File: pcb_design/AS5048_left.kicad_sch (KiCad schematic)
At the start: 6 parts, among them J5 AS5600_Right, U7 AS5048B-HTSP

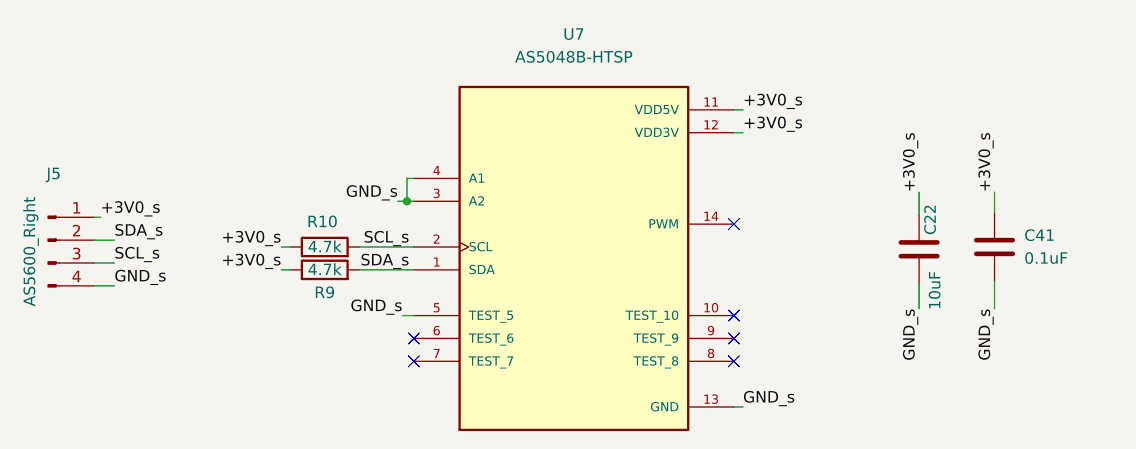
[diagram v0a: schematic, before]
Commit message: modified capacitors for encoders
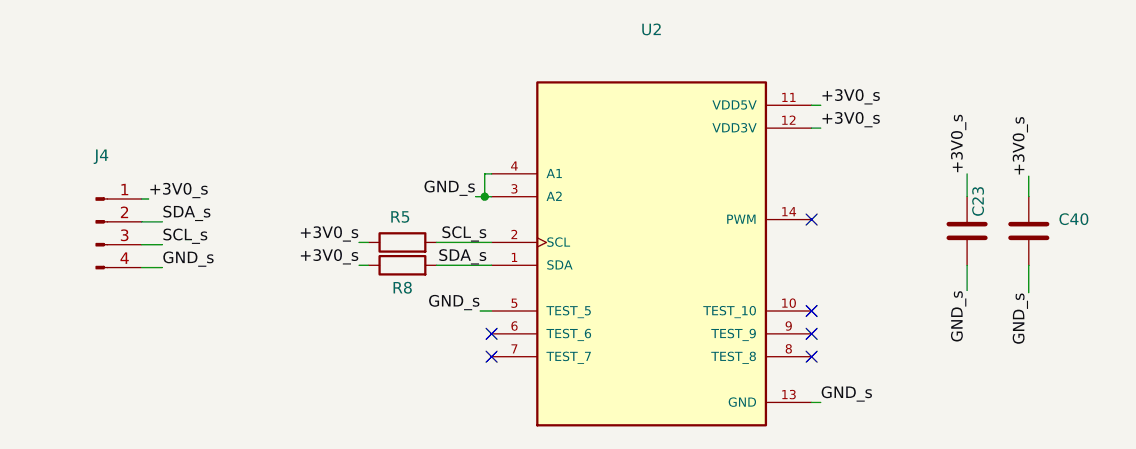
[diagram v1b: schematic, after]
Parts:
- removed C22: 10uF, Capacitor_SMD:C_0603_1608Metric, symbol Device:C
- removed C41: 0.1uF, Capacitor_SMD:C_0402_1005Metric, symbol Device:C
- removed J5: AS5600_Right, mushak_mount_footprint:STAND_SLAVE_04, symbol Connector:Conn_01x04_Male
- removed R10, R9: 4.7k, Resistor_SMD:R_0402_1005Metric, symbol Device:R
- removed U7: AS5048B-HTSP, AS5048B-HTSP:SOP65P640X120-14N, symbol AS5048B-HTSP:AS5048B-HTSP
- added C23, C40: (no value), symbol Device:C
- added J4: (no value), symbol Connector:Conn_01x04_Male
- added R5, R8: (no value), symbol Device:R
- added U2: (no value), symbol AS5048B-HTSP:AS5048B-HTSP
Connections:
- net +3V0_s: now also C23.2, C40.1, J4.1 (Pin_1), R5.1, R8.1, U2.11 (VDD5V), U2.12 (VDD3V)
- net GND_s: now also C23.1, C40.2, J4.4 (Pin_4), U2.13 (GND), U2.3 (A2), U2.4 (A1), U2.5 (TEST_5)
- net SCL_s: now also J4.3 (Pin_3), R5.2, U2.2 (SCL)
- net SDA_s: now also J4.2 (Pin_2), R8.2, U2.1 (SDA)

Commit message: Add resistors between MOSFET gate
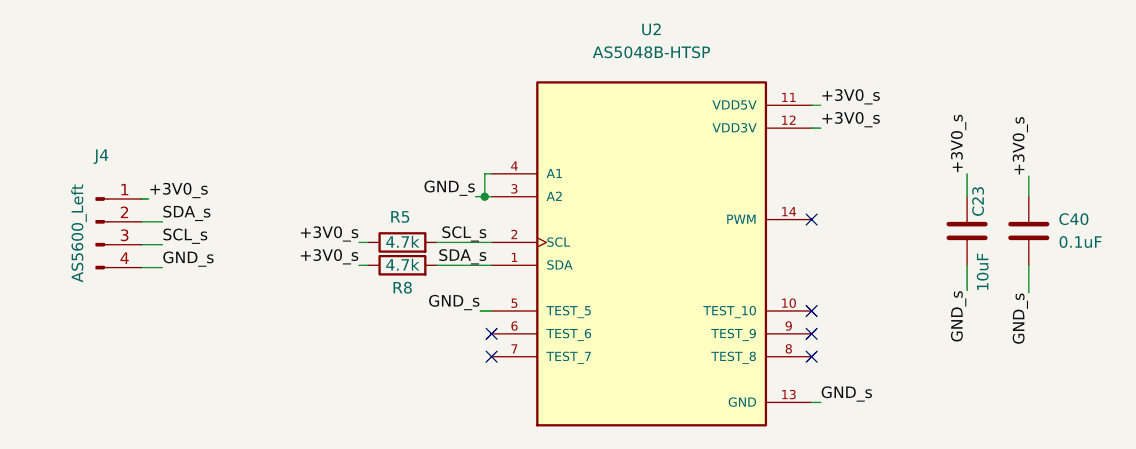
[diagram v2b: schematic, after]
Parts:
- C23: value (none) -> 10uF; footprint (none) -> Capacitor_SMD:C_0603_1608Metric
- C40: value (none) -> 0.1uF; footprint (none) -> Capacitor_SMD:C_0402_1005Metric
- J4: value (none) -> AS5600_Left; footprint (none) -> mushak_mount_footprint:STAND_SLAVE_04
- R5, R8: value (none) -> 4.7k; footprint (none) -> Resistor_SMD:R_0402_1005Metric
- U2: value (none) -> AS5048B-HTSP; footprint (none) -> AS5048B-HTSP:SOP65P640X120-14N
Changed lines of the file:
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@@
     (in_bom yes) (on_board yes)
     (property "Reference" "C23" (id 0) (at 208.28 92.964 90))
-    (property "Value" "" (id 1) (at 208.788 100.838 90))
-    (property "Footprint" "" (id 2) (at 206.0448 92.456 0)
+    (property "Value" "10uF" (id 1) (at 208.788 100.838 90))
+    (property "Footprint" "Capacitor_SMD:C_0603_1608Metric" (id 2) (at 206.0448 92.456 0)
       (effects (font (size 1.27 1.27)) hide)
     )
@@
       (effects (font (size 1.27 1.27)) (justify left))
     )
-    (property "Value" "" (id 1) (at 217.17 97.5359 0)
+    (property "Value" "0.1uF" (id 1) (at 217.17 97.5359 0)
       (effects (font (size 1.27 1.27)) (justify left))
     )
-    (property "Footprint" "" (id 2) (at 214.8332 100.076 0)
+    (property "Footprint" "Capacitor_SMD:C_0402_1005Metric" (id 2) (at 214.8332 100.076 0)
       (effects (font (size 1.27 1.27)) hide)
     )
@@
     (in_bom yes) (on_board yes) (fields_autoplaced)
     (property "Reference" "U2" (id 0) (at 171.958 73.914 0))
-    (property "Value" "" (id 1) (at 171.958 76.454 0))
-    (property "Footprint" "" (id 2) (at 171.958 97.536 0)
+    (property "Value" "AS5048B-HTSP" (id 1) (at 171.958 76.454 0))
+    (property "Footprint" "AS5048B-HTSP:SOP65P640X120-14N" (id 2) (at 171.958 97.536 0)
       (effects (font (size 1.27 1.27)) (justify left bottom) hide)
     )
@@
     (in_bom yes) (on_board yes)
     (property "Reference" "R8" (id 0) (at 144.272 102.616 90))
-    (property "Value" "" (id 1) (at 144.272 100.076 90))
-    (property "Footprint" "" (id 2) (at 144.272 101.854 90)
+    (property "Value" "4.7k" (id 1) (at 144.272 100.076 90))
+    (property "Footprint" "Resistor_SMD:R_0402_1005Metric" (id 2) (at 144.272 101.854 90)
       (effects (font (size 1.27 1.27)) hide)
     )
@@
     (in_bom yes) (on_board yes)
     (property "Reference" "J4" (id 0) (at 110.871 87.884 0))
-    (property "Value" "" (id 1) (at 108.204 96.52 90))
-    (property "Footprint" "" (id 2) (at 110.236 95.25 0)
+    (property "Value" "AS5600_Left" (id 1) (at 108.204 96.52 90))
+    (property "Footprint" "mushak_mount_footprint:STAND_SLAVE_04" (id 2) (at 110.236 95.25 0)
       (effects (font (size 1.27 1.27)) hide)
     )
@@
     (in_bom yes) (on_board yes)
     (property "Reference" "R5" (id 0) (at 144.018 94.742 90))
-    (property "Value" "" (id 1) (at 144.272 97.536 90))
-    (property "Footprint" "" (id 2) (at 144.272 99.314 90)
+    (property "Value" "4.7k" (id 1) (at 144.272 97.536 90))
+    (property "Footprint" "Resistor_SMD:R_0402_1005Metric" (id 2) (at 144.272 99.314 90)
       (effects (font (size 1.27 1.27)) hide)
     )

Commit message: Update Mushak PCB design to include new features (#5)
* Update mushak PCB with new changes
* Add AMS1117 as 3.3v regulator
* Add new alternate placement for IR sensors
* Add new 3.3v compatible ToF sensor
* Update gerber files

* Add changes to silkscreen and filter capacitors
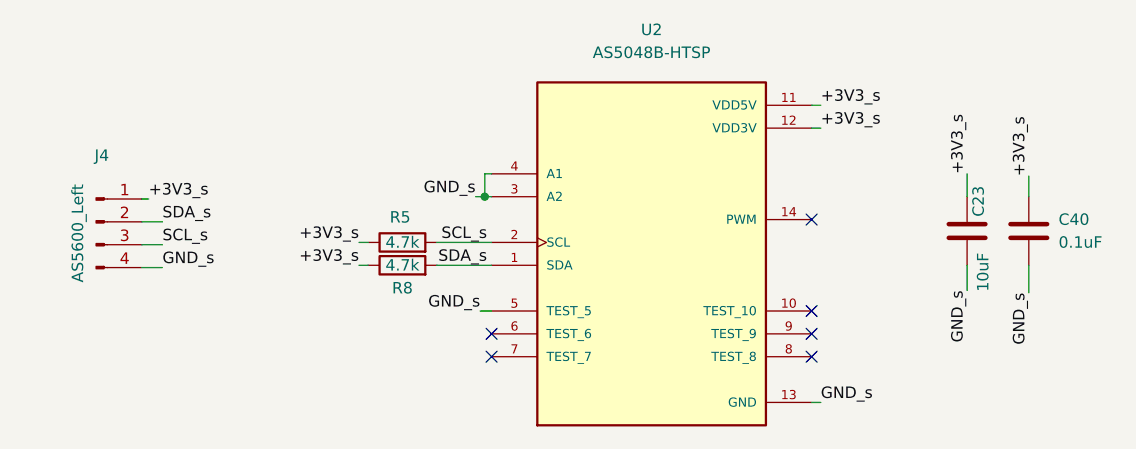
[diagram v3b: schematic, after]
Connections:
- net +3V0_s renamed +3V3_s
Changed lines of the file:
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@@
     (effects (font (size 1.27 1.27)) (justify right bottom))
   )
-  (label "+3V0_s" (at 190.754 82.296 0)
+  (label "+3V3_s" (at 190.754 82.296 0)
     (effects (font (size 1.27 1.27)) (justify left bottom))
   )
@@
     (effects (font (size 1.27 1.27)) (justify right bottom))
   )
-  (label "+3V0_s" (at 207.01 89.916 90)
+  (label "+3V3_s" (at 207.01 89.916 90)
     (effects (font (size 1.27 1.27)) (justify left bottom))
   )
-  (label "+3V0_s" (at 190.754 84.836 0)
+  (label "+3V3_s" (at 190.754 84.836 0)
     (effects (font (size 1.27 1.27)) (justify left bottom))
   )
@@
     (effects (font (size 1.27 1.27)) (justify left bottom))
   )
-  (label "+3V0_s" (at 139.446 100.076 180)
+  (label "+3V3_s" (at 139.446 100.076 180)
     (effects (font (size 1.27 1.27)) (justify right bottom))
   )
-  (label "+3V0_s" (at 116.078 92.71 0)
+  (label "+3V3_s" (at 116.078 92.71 0)
     (effects (font (size 1.27 1.27)) (justify left bottom))
   )
-  (label "+3V0_s" (at 139.446 97.536 180)
+  (label "+3V3_s" (at 139.446 97.536 180)
     (effects (font (size 1.27 1.27)) (justify right bottom))
   )
-  (label "+3V0_s" (at 213.868 90.17 90)
+  (label "+3V3_s" (at 213.868 90.17 90)
     (effects (font (size 1.27 1.27)) (justify left bottom))
   )
